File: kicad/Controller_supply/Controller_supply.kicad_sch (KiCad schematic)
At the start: 10 parts, among them J1 Conn_01x03_Pin, J2 Conn_01x06_Pin, J3 Conn_01x04_Pin, U1 MC7824, U2 MC7924

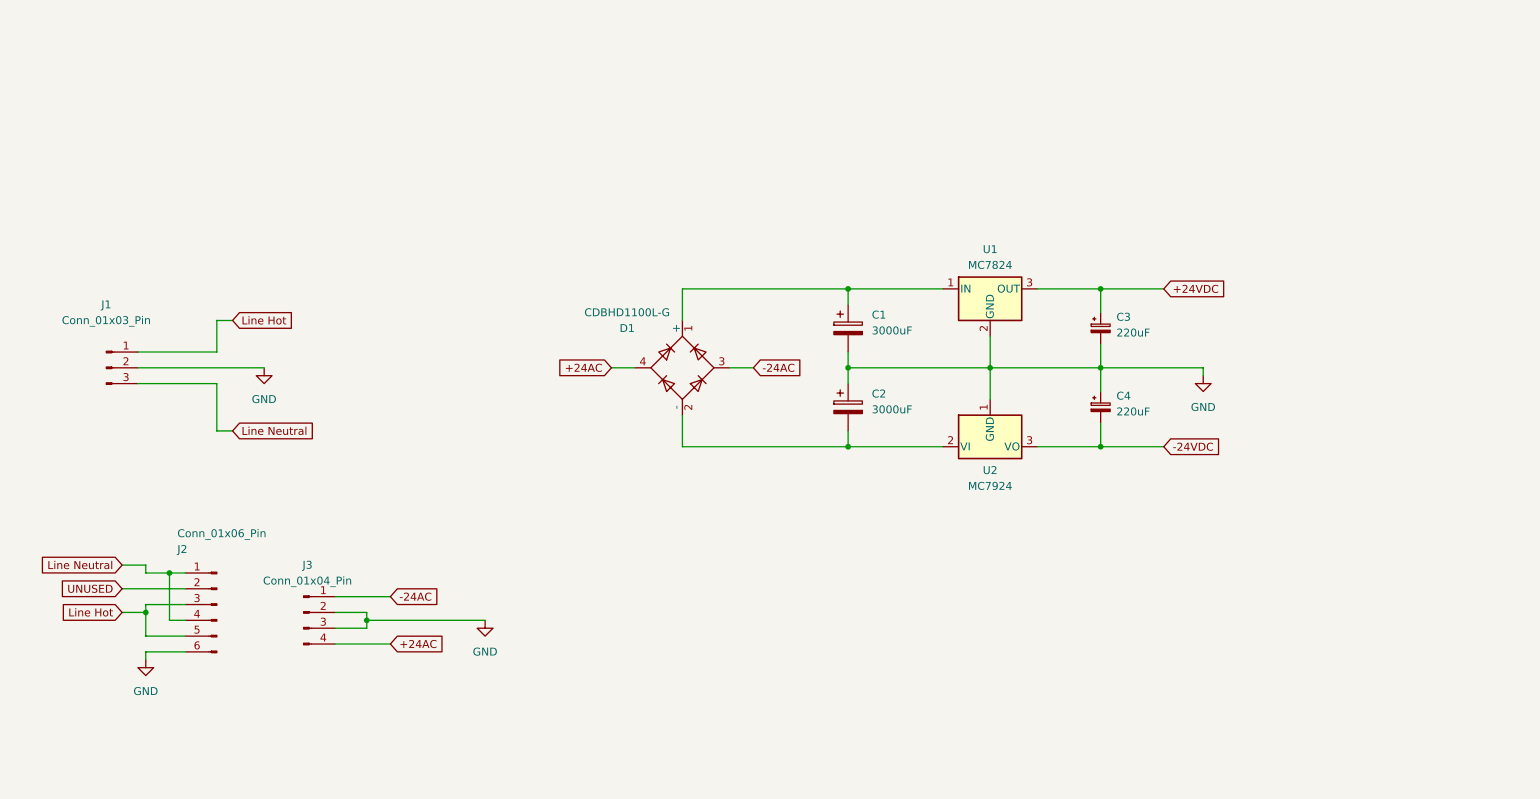
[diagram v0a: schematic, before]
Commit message: 15V output modification
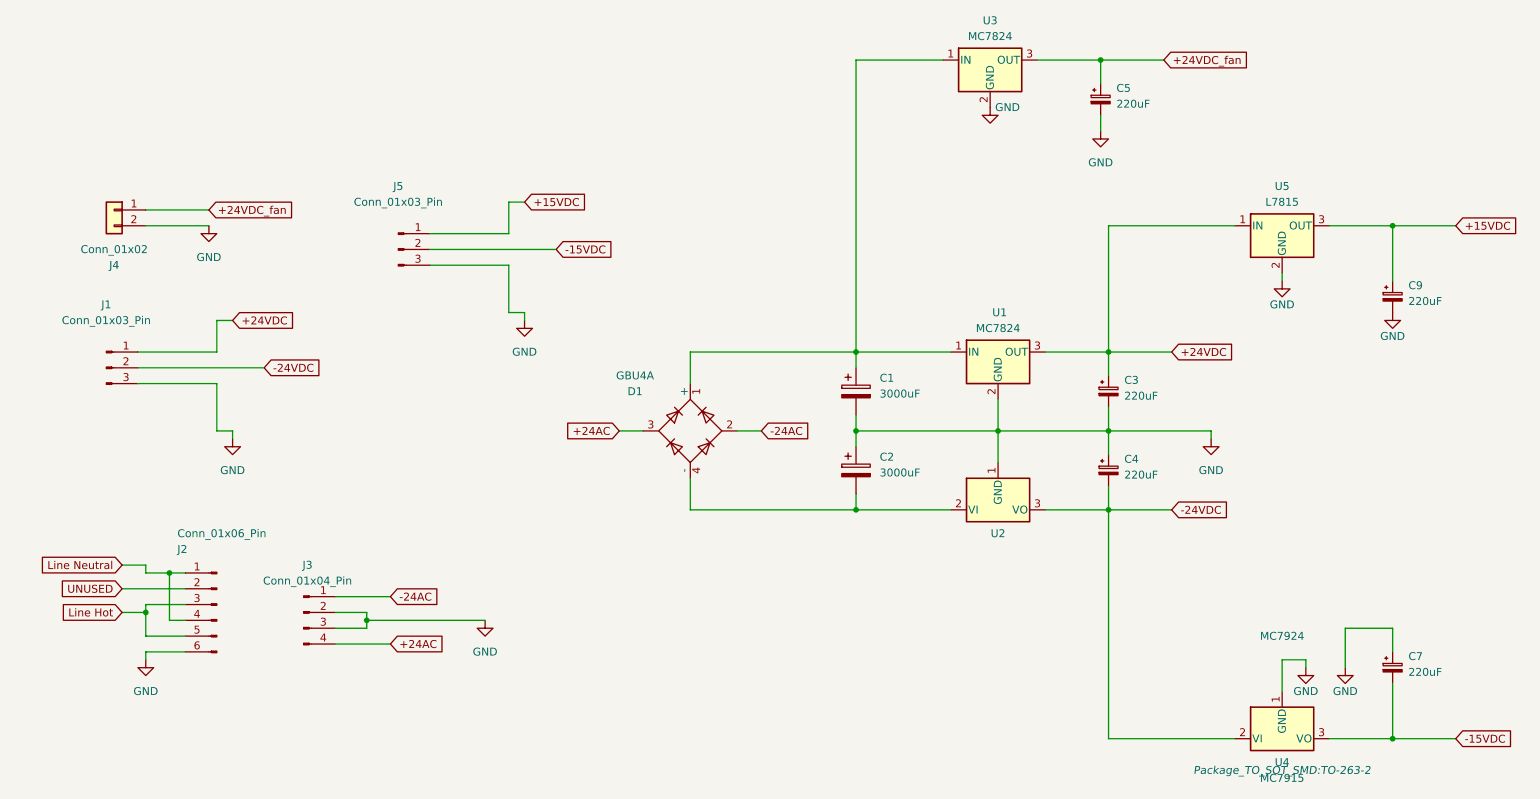
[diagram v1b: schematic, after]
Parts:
- added C5, C7, C9: 220uF, Capacitor_SMD:CP_Elec_10x10.5, symbol Device:C_Polarized_Small
- added J4: Conn_01x02, Connector_THT:Generic_7x7.5mm-footprt_1x02_P3.50mm_Horizontal, symbol Connector_Generic:Conn_01x02
- added J5: Conn_01x03_Pin, Connector_Phoenix_GMSTB:PhoenixContact_GMSTBA_2,5_3-G-7,62_1x03_P7.62mm_Horizontal, symbol Connector:Conn_01x03_Pin
- added U3: MC7824, Package_TO_SOT_SMD:TO-263-2, symbol Regulator_Linear:L7824
- added U4: MC7915, Package_TO_SOT_SMD:TO-263-2, symbol Regulator_Linear:MC7915
- added U5: L7815, Package_TO_SOT_SMD:TO-263-2, symbol Regulator_Linear:L7815
- D1: value CDBHD1100L-G -> GBU4A; footprint Package_TO_SOT_SMD:TO-269AA -> Diode_THT:Diode_Bridge_Vishay_GBU; symbol Diode_Bridge:ABS2 -> Diode_Bridge:GBU4A; DIGIKEY PARTNO 641-1209-1-ND -> GBU4A-ND; MPN CDBHD1100L-G -> GBU4A
- J1: footprint Connector_THT:CONN_1985205 -> Connector_Phoenix_GMSTB:PhoenixContact_GMSTBA_2,5_3-G-7,62_1x03_P7.62mm_Horizontal
- J3: footprint (none) -> Connector_THT:Generic_pin-to-housing_1x04_P5.00mm_Horizontal
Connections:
- net +24AC: now also D1.3; no longer D1.4
- net +24VDC: now also J1.1 (Pin_1), U5.1 (IN)
- net -24AC: now also D1.2; no longer D1.3
- net -24VDC: now also J1.2 (Pin_2), U4.2 (VI)
- net GND: now also J1.3 (Pin_3), C5.2, C7.1, C9.2, J4.2 (Pin_2), J5.3 (Pin_3), U3.2 (GND), U4.1 (GND), U5.2 (GND); no longer J1.2 (Pin_2)
- net Line Hot: no longer J1.1 (Pin_1)
- net Line Neutral: no longer J1.3 (Pin_3)
- net at C1.1, D1.1 (+), U1.1 (IN): now also U3.1 (IN)
- net at C2.2, U2.2 (VI): now also D1.4 (-); no longer D1.2 (-)
- new net +15VDC: C9.1, J5.1 (Pin_1), U5.3 (OUT)
- new net +24VDC_fan: C5.1, J4.1 (Pin_1), U3.3 (OUT)
- new net -15VDC: C7.2, J5.2 (Pin_2), U4.3 (VO)
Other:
- moved on the sheet: C1, C2, C3, C4, D1, U1, U2
